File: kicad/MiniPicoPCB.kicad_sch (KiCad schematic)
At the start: 13 parts, among them J1 Screw_Terminal_01x05, J10 Screw_Terminal_01x05, J11 Conn_01x20_Socket, J12 Conn_01x20_Socket, J2 Screw_Terminal_01x05, J3 Screw_Terminal_01x05, J4 Screw_Terminal_01x05, J5 Screw_Terminal_01x05, J6 Screw_Terminal_01x05, J7 Screw_Terminal_01x05, J8 Screw_Terminal_01x05, J9 Screw_Terminal_01x05

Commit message: Update schematic, PCB, assets
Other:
- note added: "MCU RP2040 limitations : Maximum current sourced per GPIO pin : < 12mA Maximum total current output by ALL pins combined : < 250mA"
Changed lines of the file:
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@@
 	(title_block
 		(title "${TITLE_NAME}")
-		(date "2026-07-22")
+		(date "2026-09-21")
 		(rev "${SCHEMATIC_VERSION}")
 		(comment 2 "${PROJECT_LINK}")
 		(comment 3 "For Raspberry Pi Pico only")
+	)
+	(text "MCU RP2040 limitations :\nMaximum current sourced per GPIO pin : < 12mA\nMaximum total current output by ALL pins combined : < 250mA"
+		(exclude_from_sim no)
+		(at 101.6 36.83 0)
+		(effects
+			(font
+				(size 1.5 1.5)
+				(thickness 0.22)
+				(bold yes)
+				(color 255 0 0 1)
+			)
+			(justify left top)
+		)
 	)
 	(text "(for reference only)"
@@
 	)
 	(junction
-		(at 175.26 62.23)
-		(diameter 0)
-		(color 0 0 0 0)
-	)
-	(junction
 		(at 100.33 111.76)
 		(diameter 0)
@@
 	)
 	(junction
+		(at 176.53 62.23)
+		(diameter 0)
+		(color 0 0 0 0)
+	)
+	(junction
 		(at 100.33 86.36)
 		(diameter 0)
@@
 	(wire
 		(pts
+			(xy 156.21 57.15) (xy 161.29 57.15)
+		)
+		(stroke
+			(width 0)
+			(type default)
+		)
+	)
+	(wire
+		(pts
 			(xy 99.06 68.58) (xy 101.6 68.58)
 		)
@@
 	(wire
 		(pts
-			(xy 175.26 62.23) (xy 181.61 62.23)
-		)
-		(stroke
-			(width 0)
-			(type default)
-		)
-	)
-	(wire
-		(pts
 			(xy 99.06 111.76) (xy 100.33 111.76)
 		)
@@
 	(wire
 		(pts
-			(xy 175.26 59.69) (xy 175.26 62.23)
+			(xy 176.53 53.34) (xy 176.53 62.23)
 		)
 		(stroke
@@
 	(wire
 		(pts
-			(xy 163.83 62.23) (xy 175.26 62.23)
+			(xy 163.83 62.23) (xy 176.53 62.23)
 		)
 		(stroke
@@
 	(wire
 		(pts
-			(xy 181.61 53.34) (xy 181.61 62.23)
+			(xy 187.96 53.34) (xy 187.96 62.23)
 		)
 		(stroke
@@
 	(wire
 		(pts
-			(xy 161.29 48.26) (xy 161.29 57.15)
+			(xy 156.21 53.34) (xy 156.21 57.15)
 		)
 		(stroke
@@
 	(wire
 		(pts
-			(xy 167.64 54.61) (xy 167.64 57.15)
+			(xy 167.64 53.34) (xy 167.64 57.15)
 		)
 		(stroke
@@
 		(pts
 			(xy 160.02 116.84) (xy 165.1 116.84)
+		)
+		(stroke
+			(width 0)
+			(type default)
+		)
+	)
+	(wire
+		(pts
+			(xy 176.53 62.23) (xy 187.96 62.23)
 		)
 		(stroke
@@
 	(symbol
 		(lib_id "power:PWR_FLAG")
-		(at 161.29 48.26 0)
+		(at 156.21 53.34 0)
 		(unit 1)
 		(exclude_from_sim no)
@@
 		(fields_autoplaced yes)
 		(property "Reference" "#FLG01"
-			(at 161.29 46.355 0)
+			(at 156.21 51.435 0)
 			(effects
 				(font
@@
 		)
 		(property "Value" "PWR_FLAG"
-			(at 161.29 43.18 0)
+			(at 156.21 48.26 0)
 			(effects
 				(font
@@
 		)
 		(property "Footprint" ""
-			(at 161.29 48.26 0)
+			(at 156.21 53.34 0)
 			(effects
 				(font
@@
 		)
 		(property "Datasheet" "~"
-			(at 161.29 48.26 0)
+			(at 156.21 53.34 0)
 			(effects
 				(font
@@
 		)
 		(property "Description" "Special symbol for telling ERC where power comes from"
-			(at 161.29 48.26 0)
+			(at 156.21 53.34 0)
 			(effects
 				(font
@@
 		)
 		(property "Purpose" ""
-			(at 161.29 48.26 0)
+			(at 156.21 53.34 0)
 			(effects
 				(font
@@
 	(symbol
 		(lib_id "power:PWR_FLAG")
-		(at 181.61 53.34 0)
+		(at 187.96 53.34 0)
 		(unit 1)
 		(exclude_from_sim no)
@@
 		(fields_autoplaced yes)
 		(property "Reference" "#FLG02"
-			(at 181.61 51.435 0)
+			(at 187.96 51.435 0)
 			(effects
 				(font
@@
 		)
 		(property "Value" "PWR_FLAG"
-			(at 181.61 48.26 0)
+			(at 187.96 48.26 0)
 			(effects
 				(font
@@
 		)
 		(property "Footprint" ""
-			(at 181.61 53.34 0)
+			(at 187.96 53.34 0)
 			(effects
 				(font
@@
 		)
 		(property "Datasheet" "~"
-			(at 181.61 53.34 0)
+			(at 187.96 53.34 0)
 			(effects
 				(font
@@
 		)
 		(property "Description" "Special symbol for telling ERC where power comes from"
-			(at 181.61 53.34 0)
+			(at 187.96 53.34 0)
 			(effects
 				(font
@@
 		)
 		(property "Purpose" ""
-			(at 181.61 53.34 0)
+			(at 187.96 53.34 0)
 			(effects
 				(font
@@
 	(symbol
 		(lib_id "power:GND")
-		(at 167.64 54.61 180)
+		(at 167.64 53.34 180)
 		(unit 1)
 		(exclude_from_sim no)
@@
 		(fields_autoplaced yes)
 		(property "Reference" "#PWR08"
+			(at 167.64 46.99 0)
+			(effects
+				(font
+					(size 1.27 1.27)
+				)
+				(hide yes)
+			)
+		)
+		(property "Value" "GND"
 			(at 167.64 48.26 0)
 			(effects
@@
 					(size 1.27 1.27)
 				)
-				(hide yes)
-			)
-		)
-		(property "Value" "GND"
-			(at 167.64 49.53 0)
-			(effects
-				(font
-					(size 1.27 1.27)
-				)
 			)
 		)
 		(property "Footprint" ""
-			(at 167.64 54.61 0)
+			(at 167.64 53.34 0)
 			(effects
 				(font
@@
 		)
 		(property "Datasheet" ""
-			(at 167.64 54.61 0)
+			(at 167.64 53.34 0)
 			(effects
 				(font
@@
 		)
 		(property "Description" "Power symbol creates a global label with name \"GND\" , ground"
-			(at 167.64 54.61 0)
+			(at 167.64 53.34 0)
 			(effects
 				(font
@@
 		)
 		(property "Purpose" ""
-			(at 167.64 54.61 0)
+			(at 167.64 53.34 0)
 			(effects
 				(font
@@
 	(symbol
 		(lib_id "power:+3.3V")
-		(at 175.26 59.69 0)
+		(at 176.53 53.34 0)
 		(unit 1)
 		(exclude_from_sim no)
@@
 		(fields_autoplaced yes)
 		(property "Reference" "#PWR09"
-			(at 175.26 63.5 0)
+			(at 176.53 57.15 0)
 			(effects
 				(font
@@
 		)
 		(property "Value" "+3.3V"
-			(at 175.26 54.61 0)
+			(at 176.53 48.26 0)
 			(effects
 				(font
@@
 		)
 		(property "Footprint" ""
-			(at 175.26 59.69 0)
+			(at 176.53 53.34 0)
 			(effects
 				(font
@@
 		)
 		(property "Datasheet" ""
-			(at 175.26 59.69 0)
+			(at 176.53 53.34 0)
 			(effects
 				(font
@@
 		)
 		(property "Description" "Power symbol creates a global label with name \"+3.3V\""
-			(at 175.26 59.69 0)
+			(at 176.53 53.34 0)
 			(effects
 				(font
@@
 		)
 		(property "Purpose" ""
-			(at 175.26 59.69 0)
-			(effects
-				(font
+			(at 176.53 53.34 0)
+			(effects
+				(font

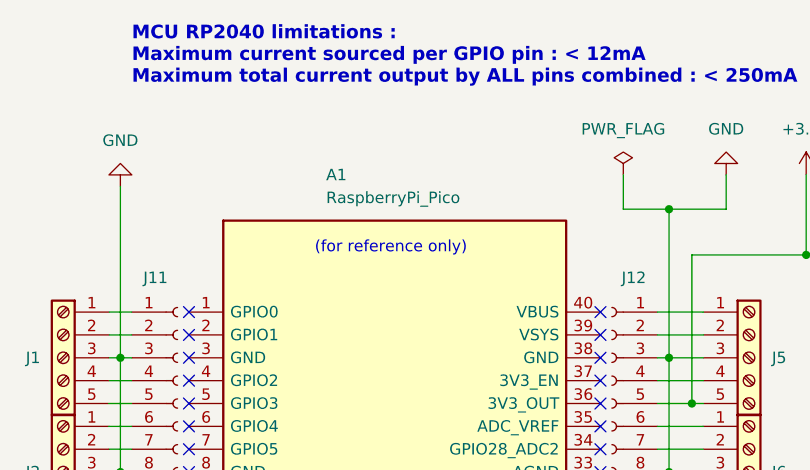
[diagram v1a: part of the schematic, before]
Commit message: Update footprint warning
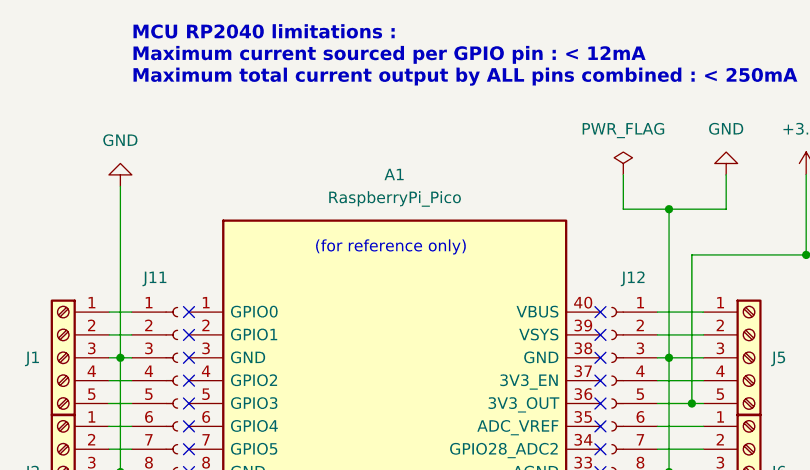
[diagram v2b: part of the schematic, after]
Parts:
- removed A1: RaspberryPi_Pico, Module:RaspberryPi_Pico_Common_Unspecified, symbol MCU_Module:RaspberryPi_Pico
- added A1: RaspberryPi_Pico, Module:RaspberryPi_Pico_Common_Unspecified, symbol MiniPicoPCB:RaspberryPi_Pico
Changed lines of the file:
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@@
 	(title_block
 		(title "${TITLE_NAME}")
-		(date "2026-09-21")
+		(date "2026-10-06")
 		(rev "${SCHEMATIC_VERSION}")
 		(comment 2 "${PROJECT_LINK}")
@@
 			(width 0)
 			(type default)
-		)
-	)
-	(symbol
-		(lib_id "MCU_Module:RaspberryPi_Pico")
-		(at 130.81 92.71 0)
-		(unit 1)
-		(exclude_from_sim no)
-		(in_bom no)
-		(on_board no)
-		(dnp no)
-		(property "Reference" "A1"
-			(at 123.19 53.34 0)
-			(effects
-				(font
-					(size 1.27 1.27)
-				)
-				(justify left)
-			)
-		)
-		(property "Value" "RaspberryPi_Pico"
-			(at 123.19 55.88 0)
-			(effects
-				(font
-					(size 1.27 1.27)
-				)
-				(justify left)
-			)
-		)
-		(property "Footprint" "Module:RaspberryPi_Pico_Common_Unspecified"
-			(at 130.81 128.27 0)
-			(effects
-				(font
-					(size 1.27 1.27)
-				)
-				(hide yes)
-			)
-		)
-		(property "Datasheet" "https://datasheets.raspberrypi.com/pico/pico-datasheet.pdf"
-			(at 130.81 130.81 0)
-			(effects
-				(font
-					(size 1.27 1.27)
-				)
-				(hide yes)
-			)
-		)
-		(property "Description" "Versatile and inexpensive microcontroller module powered by RP2040 dual-core Arm Cortex-M0+ processor up to 133 MHz, 264kB SRAM, 2MB QSPI flash; also supports Raspberry Pi Pico 2"
-			(at 130.81 133.35 0)
-			(effects
-				(font
-					(size 1.27 1.27)
-				)
-				(hide yes)
-			)
-		)
-		(pin "35"
-		)
-		(pin "34"
-		)
-		(pin "24"
-		)
-		(pin "13"
-		)
-		(pin "15"
-		)
-		(pin "31"
-		)
-		(pin "11"
-		)
-		(pin "33"
-		)
-		(pin "29"
-		)
-		(pin "32"
-		)
-		(pin "18"
-		)
-		(pin "40"
-		)
-		(pin "19"
-		)
-		(pin "9"
-		)
-		(pin "17"
-		)
-		(pin "16"
-		)
-		(pin "22"
-		)
-		(pin "21"
-		)
-		(pin "36"
-		)
-		(pin "3"
-		)
-		(pin "2"
-		)
-		(pin "1"
-		)
-		(pin "37"
-		)
-		(pin "23"
-		)
-		(pin "39"
-		)
-		(pin "38"
-		)
-		(pin "20"
-		)
-		(pin "26"
-		)
-		(pin "5"
-		)
-		(pin "4"
-		)
-		(pin "6"
-		)
-		(pin "7"
-		)
-		(pin "14"
-		)
-		(pin "12"
-		)
-		(pin "10"
-		)
-		(pin "27"
-		)
-		(pin "28"
-		)
-		(pin "25"
-		)
-		(pin "30"
-		)
-		(pin "8"
-		)
-		(instances
-			(project "MiniPicoPCB"
-				(path "/86644c21-3caa-4c6d-8c75-c0a1b6d5c30d"
-					(reference "A1")
-					(unit 1)
-				)
-			)
 		)
 	)
@@
 					(unit 1)
 				)
+			)
+		)
+	)
+	(symbol
+		(lib_id "MiniPicoPCB:RaspberryPi_Pico")
+		(at 130.81 92.71 0)
+		(unit 1)
+		(exclude_from_sim no)
+		(in_bom no)
+		(on_board no)
+		(dnp no)
+		(fields_autoplaced yes)
+		(property "Reference" "A1"
+			(at 130.81 53.34 0)
+			(effects
+				(font
+					(size 1.27 1.27)
+				)
+			)
+		)
+		(property "Value" "RaspberryPi_Pico"
+			(at 130.81 55.88 0)
+			(effects
+				(font
+					(size 1.27 1.27)
+				)
+			)
+		)
+		(property "Footprint" "Module:RaspberryPi_Pico_Common_Unspecified"
+			(at 130.81 128.27 0)
+			(effects
+				(font
+					(size 1.27 1.27)
+				)
+				(hide yes)
+			)
+		)
+		(property "Datasheet" "https://datasheets.raspberrypi.com/pico/pico-datasheet.pdf"
+			(at 130.81 130.81 0)
+			(effects
+				(font
+					(size 1.27 1.27)
+				)
+				(hide yes)
+			)
+		)
+		(property "Description" "Versatile and inexpensive microcontroller module powered by RP2040 dual-core Arm Cortex-M0+ processor up to 133 MHz, 264kB SRAM, 2MB QSPI flash; also supports Raspberry Pi Pico 2"
+			(at 130.81 133.35 0)
+			(effects
+				(font
+					(size 1.27 1.27)
+				)
+				(hide yes)
+			)
+		)
+		(pin "31"
+		)
+		(pin "30"
+		)
+		(pin "13"
+		)
+		(pin "29"
+		)
+		(pin "40"
+		)
+		(pin "32"
+		)
+		(pin "15"
+		)
+		(pin "37"
+		)
+		(pin "7"
+		)
+		(pin "2"
+		)
+		(pin "1"
+		)
+		(pin "3"
+		)
+		(pin "6"
+		)
+		(pin "16"
+		)
+		(pin "9"
+		)
+		(pin "23"
+		)
+		(pin "11"
+		)
+		(pin "22"
+		)
+		(pin "28"
+		)
+		(pin "26"
+		)
+		(pin "24"
+		)
+		(pin "27"
+		)
+		(pin "25"
+		)
+		(pin "10"
+		)
+		(pin "19"
+		)
+		(pin "18"
+		)
+		(pin "39"
+		)
+		(pin "33"
+		)
+		(pin "35"
+		)
+		(pin "38"
+		)
+		(pin "34"
+		)
+		(pin "20"
+		)
+		(pin "14"
+		)
+		(pin "12"
+		)
+		(pin "36"
+		)
+		(pin "17"
+		)
+		(pin "8"
+		)
+		(pin "5"
+		)
+		(pin "4"
+		)
+		(pin "21"
+		)
+		(instances
+			(project "MiniPicoPCB"
+				(path "/86644c21-3caa-4c6d-8c75-c0a1b6d5c30d"
+					(reference "A1")
+					(unit 1)
+				)
